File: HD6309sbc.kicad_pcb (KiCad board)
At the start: 2 copper layers, 99.8 x 99.8 mm, 30 parts, among them J1 Conn_01x02_Male, J2 Conn_02x30_Odd_Even, J3 Conn_01x02_Male, U1 HD63C09, U10 74LS375D, U11 74HC02, U12 74AHC1G08, U13 74HC21D, U14 74HC21D, U15 74HC21D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

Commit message: fixes
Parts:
- added R3: 4.7k, Resistor_SMD:R_0805_2012Metric_Pad1.20x1.40mm_HandSolder, F.Cu at (41.7, 109.0)
- added R4: 4.7k, Resistor_SMD:R_0805_2012Metric_Pad1.20x1.40mm_HandSolder, F.Cu at (41.7, 106.4)
- added R5: 4.7k, Resistor_SMD:R_0805_2012Metric_Pad1.20x1.40mm_HandSolder, F.Cu at (41.7, 103.9)
- added R6: 4.7k, Resistor_SMD:R_0805_2012Metric_Pad1.20x1.40mm_HandSolder, F.Cu at (41.7, 101.3)
- C1, C7: footprint Capacitor_SMD:C_0402_1005Metric -> Capacitor_SMD:C_0805_2012Metric_Pad1.18x1.45mm_HandSolder
- RN1, RN2, RN3: value R_Network08 -> 4K7
- U6: value 27C256 -> 28C256
- moved C7 0.68 mm to (123.7, 41.1)
- moved C1 0.66 mm to (108.0, 41.1)
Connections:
- U6 pad 1: unconnected-(U6-Pad1) -> +5V
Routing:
- net +5V: track 494.8 -> 518.7 mm
- net ~{NMI}: track 35.3 -> 56.3 mm, vias 0 -> 1
- net ~{IRQ}: track 40.8 -> 55.4 mm, vias 0 -> 1
- net ~{HALT}: track 39.7 -> 52.5 mm, vias 1 -> 2
- net ~{FIRQ}: track 44.7 -> 57.0 mm, vias 0 -> 1
- net A8: track 189.0 -> 193.5 mm

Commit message: rework traces
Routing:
- net A11: track 183.9 -> 178.0 mm, vias 1 -> 2
- net Net-(U13-Pad9): track 85.1 -> 86.5 mm
- net A1: track 157.9 -> 159.3 mm
- net D5: track 142.2 -> 143.1 mm
- net A8: track 193.5 -> 192.9 mm
- net D6: track 143.5 -> 144.0 mm
- net A0: track 186.8 -> 187.3 mm, vias 3 -> 5
- net GND: track 624.3 -> 624.9 mm
- net D0: track 148.0 -> 148.5 mm, vias 3 -> 5
- net A14: track 173.0 -> 172.6 mm, vias 4 -> 6
- net D1: track 151.2 -> 151.0 mm, vias 2 -> 3
- net A2: track 204.9 -> 204.7 mm, vias 3 -> 4
- net D2: track 168.3 -> 168.5 mm, vias 2 -> 4
- net +5V: track 518.7 -> 518.5 mm, vias 15 -> 17
- net A6: vias 6 -> 7
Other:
- board text added: "6309 SBC Rev 1.3"

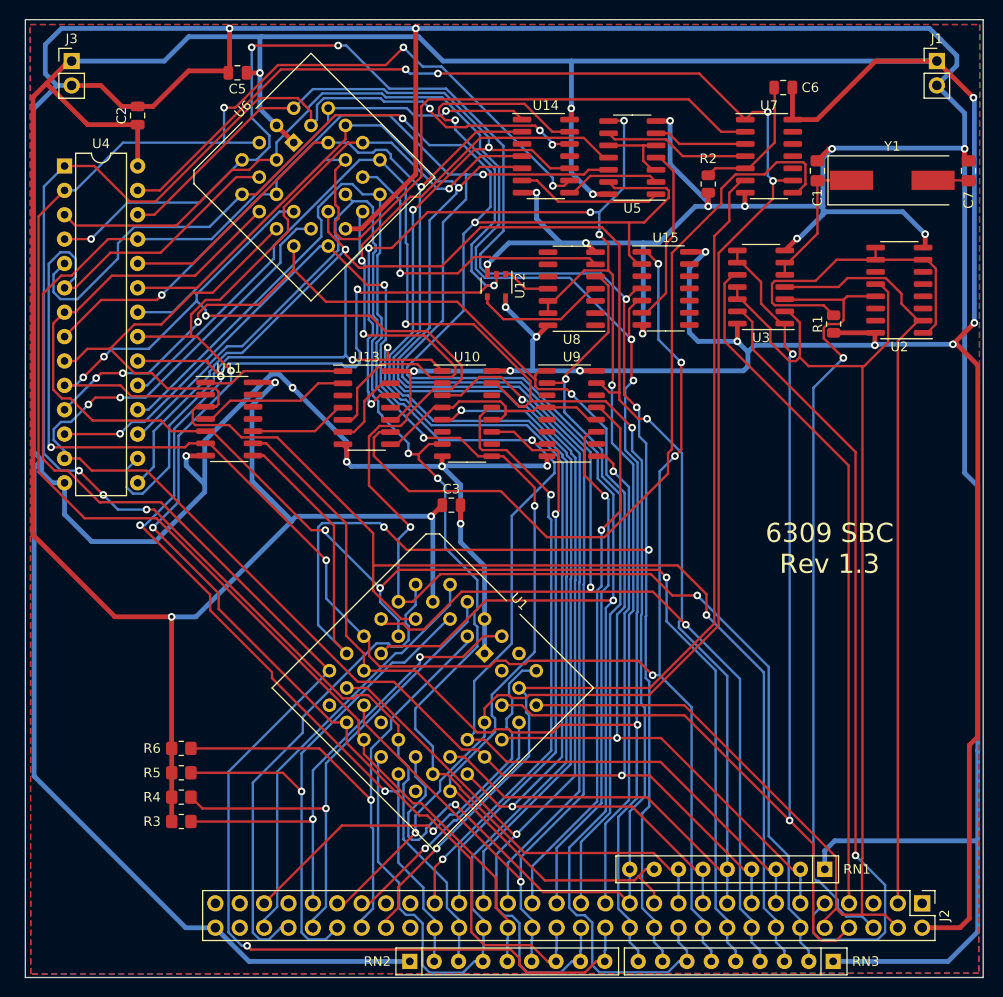
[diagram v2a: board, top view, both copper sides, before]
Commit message: use handsolder pads
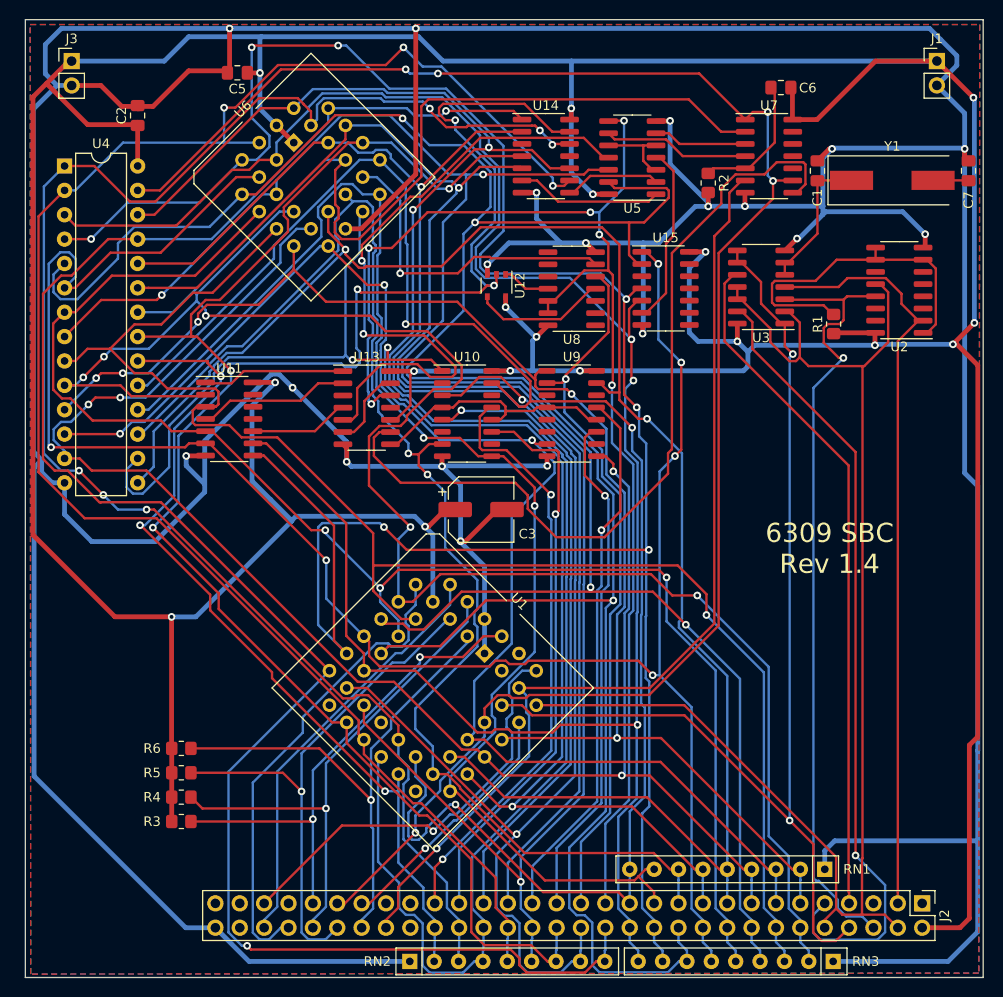
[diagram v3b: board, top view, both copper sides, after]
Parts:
- C1, C7: value 17pF -> 18pF
- C2, C5: footprint Capacitor_SMD:C_0805_2012Metric -> Capacitor_SMD:C_0805_2012Metric_Pad1.18x1.45mm_HandSolder
- C3: footprint Capacitor_SMD:C_0805_2012Metric -> Capacitor_SMD:CP_Elec_6.3x5.8
- C6: value C -> 1uF; footprint Capacitor_SMD:C_0805_2012Metric -> Capacitor_SMD:C_0805_2012Metric_Pad1.18x1.45mm_HandSolder
- R1, R2: footprint Resistor_SMD:R_0805_2012Metric -> Resistor_SMD:R_0805_2012Metric_Pad1.20x1.40mm_HandSolder
- moved C3 3.13 mm to (72.9, 76.5)
- moved C6 0.25 mm to (104.1, 32.5)
- moved R2 0.11 mm to (96.6, 42.4)
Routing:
- net GND: track 624.9 -> 629.0 mm
- net +5V: track 518.5 -> 519.6 mm
- net Net-(U13-Pad9): track 86.5 -> 87.4 mm
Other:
- board text added: "6309 SBC Rev 1.4"
- board text removed: "6309 SBC Rev 1.3"

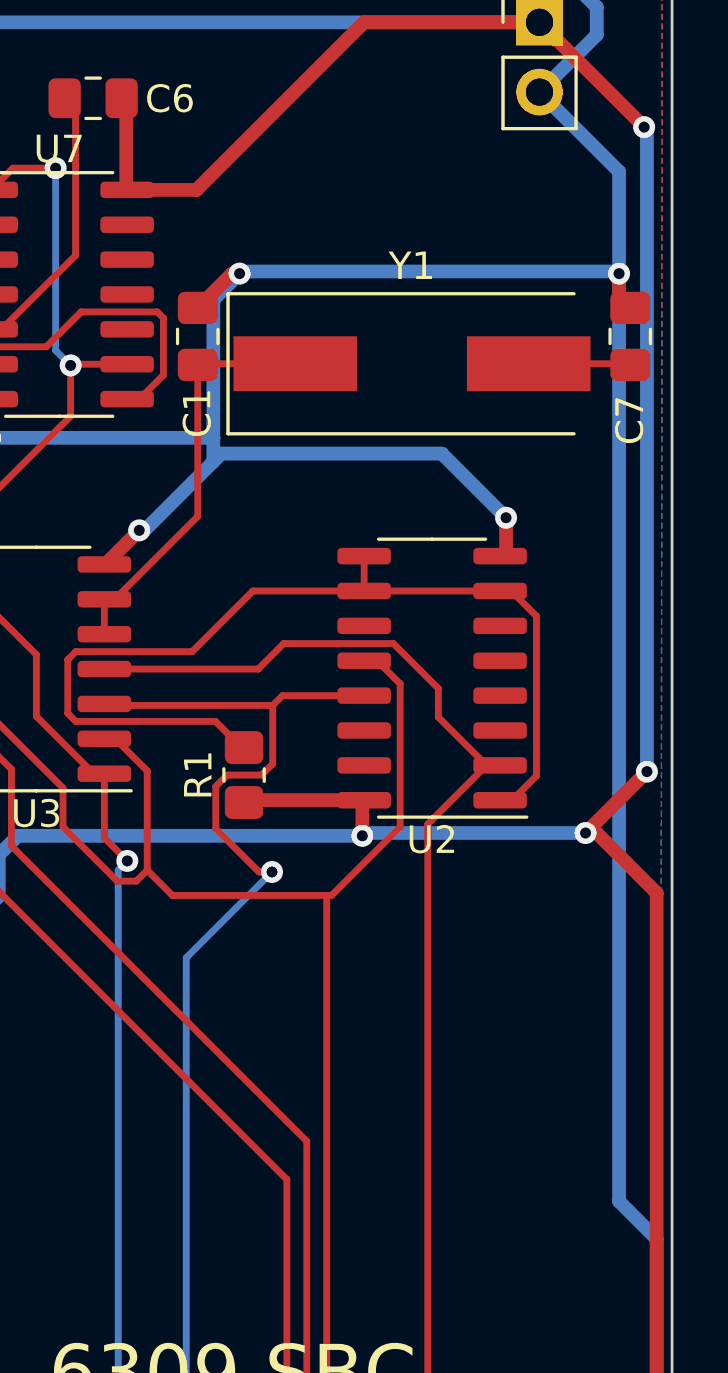
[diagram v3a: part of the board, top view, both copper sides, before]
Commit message: improve keepout around crystal
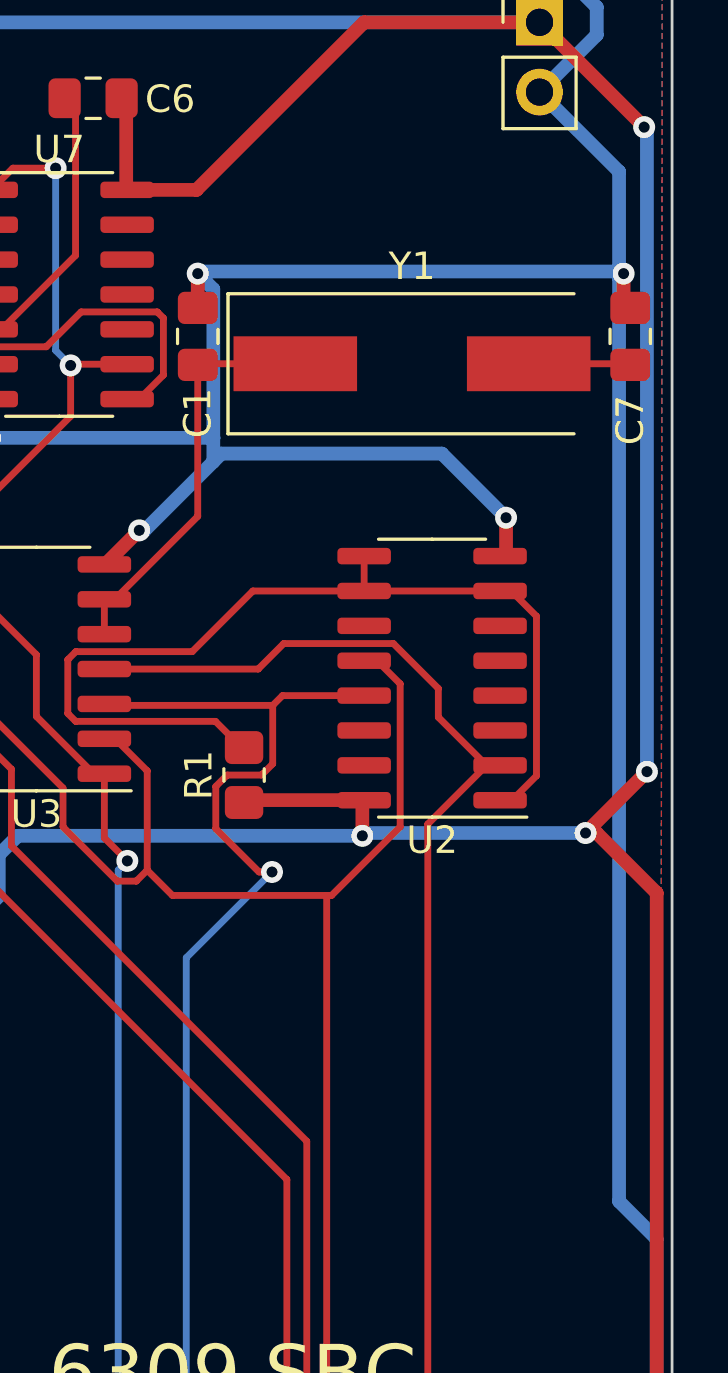
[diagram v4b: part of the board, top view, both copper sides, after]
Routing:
- net GND: track 629.0 -> 629.8 mm

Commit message: convert to discrete clock
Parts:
- removed C1, C7: 18pF, Capacitor_SMD:C_0805_2012Metric_Pad1.18x1.45mm_HandSolder
- removed R1: 2.2k, Resistor_SMD:R_0805_2012Metric_Pad1.20x1.40mm_HandSolder
- removed U2: 74HC163, Package_SO:SOIC-16_3.9x9.9mm_P1.27mm
- removed U3: 74HC02D, Package_SO:SOIC-14_3.9x8.7mm_P1.27mm
- removed Y1: 25.175MHz, Crystal:Crystal_SMD_HC49-SD
- added J4: Conn_01x06_Socket, Connector_PinSocket_2.54mm:PinSocket_1x06_P2.54mm_Vertical, F.Cu at (100.9, 78.4)
- added J5: Conn_01x06_Socket, Connector_PinSocket_2.54mm:PinSocket_1x06_P2.54mm_Vertical, F.Cu at (107.2, 50.3)
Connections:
- J2 pad 10: Clock3 -> Q
- U1 pad 39: Clock3 -> Q
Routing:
- net Q: track 0.00 -> 114.6 mm, vias 0 -> 2
- net Clock3: track 144.7 -> 61.3 mm, vias 0 -> 2
- net GND: track 629.8 -> 584.2 mm, vias 19 -> 15
- net Net-(R1-Pad2): track 36.2 -> 0.00 mm
- net Clock24: track 78.9 -> 53.1 mm, vias 0 -> 2
- net Clock6: track 82.8 -> 60.2 mm
- net ~{RESET}: track 102.5 -> 120.4 mm, vias 1 -> 3
- net Net-(C1-Pad1): track 15.0 -> 0.00 mm
- net ~{E}: track 71.7 -> 67.7 mm
- net +5V: track 519.6 -> 523.6 mm, vias 17 -> 13
- net Net-(C7-Pad1): track 3.71 -> 0.00 mm
- net E: track 114.8 -> 112.9 mm
- net ~{Q}: track 83.0 -> 84.8 mm
- net A4: track 208.1 -> 209.2 mm
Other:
- board text added: "1.5x"
- board text added: "12x"
- board text added: "24x"
- board text added: "3x"
- board text added: "6309 SBC Rev 1.5"
- board text added: "6x"
- board text added: "Clock Card"
- board text added: "E"
- board text added: "Q"
- board text added: "~{E}"
- board text added: "~{Q}"
- board text added: "~{RESET}"
- board text removed: "6309 SBC Rev 1.4"

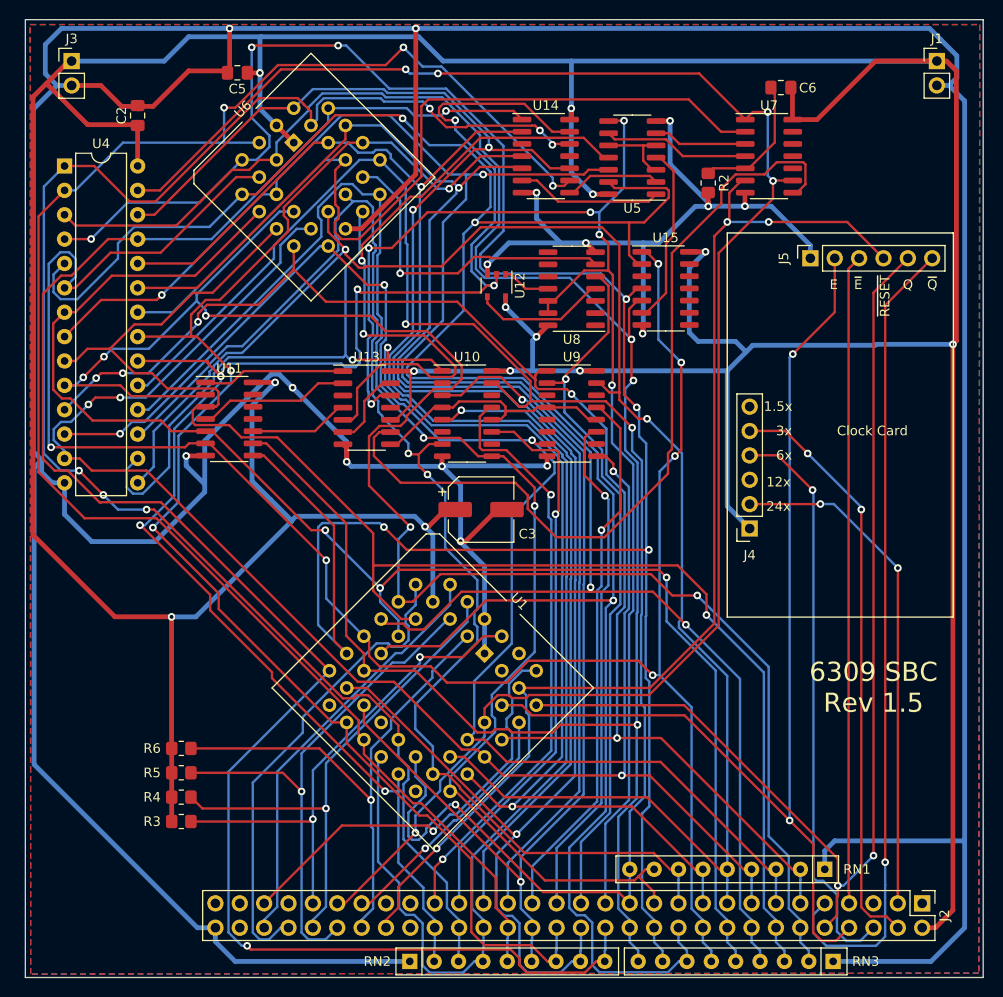
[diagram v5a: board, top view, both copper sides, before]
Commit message: add diagnostics port
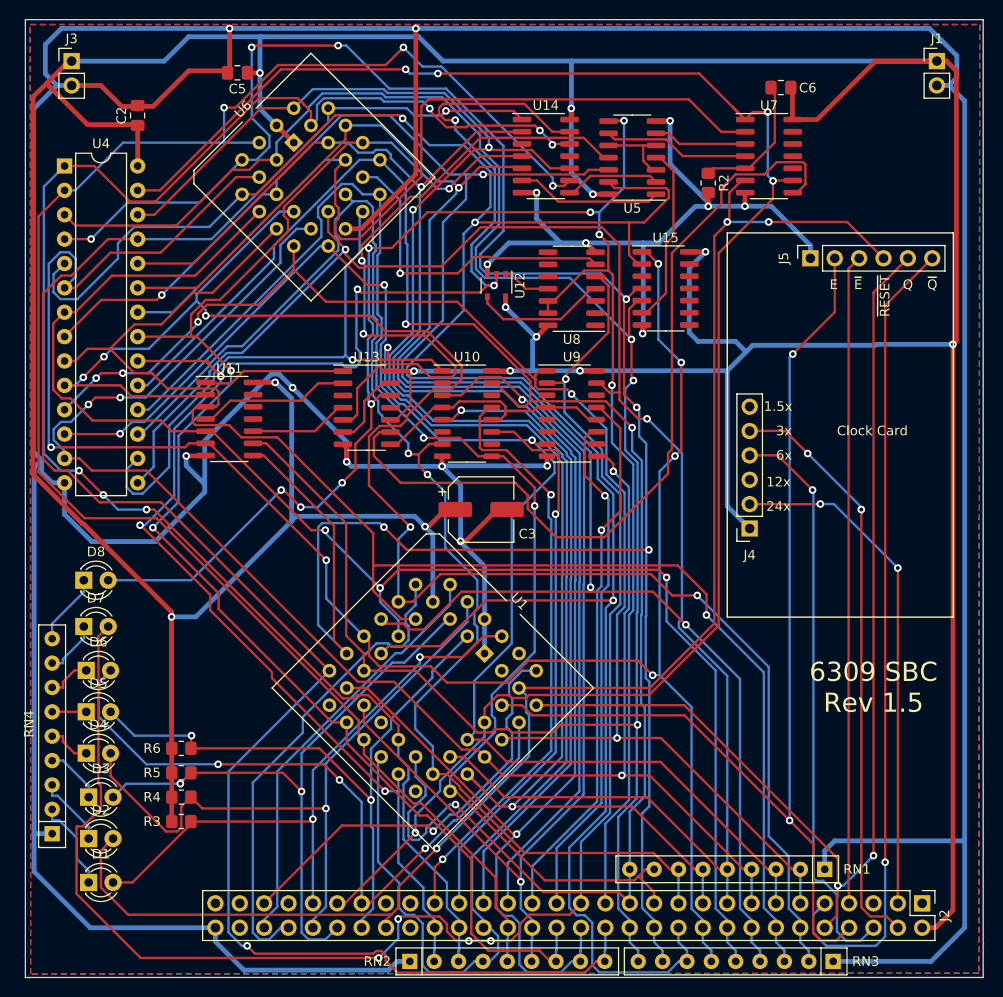
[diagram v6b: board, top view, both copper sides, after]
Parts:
- added D1: LED_Small, LED_THT:LED_D3.0mm, F.Cu at (32.0, 115.3)
- added D2: LED_Small, LED_THT:LED_D3.0mm, F.Cu at (32.0, 110.7)
- added D3: LED_Small, LED_THT:LED_D3.0mm, F.Cu at (32.0, 106.4)
- added D4: LED_Small, LED_THT:LED_D3.0mm, F.Cu at (31.7, 101.9)
- added D5: LED_Small, LED_THT:LED_D3.0mm, F.Cu at (31.7, 97.5)
- added D6: LED_Small, LED_THT:LED_D3.0mm, F.Cu at (31.7, 93.2)
- added D7: LED_Small, LED_THT:LED_D3.0mm, F.Cu at (31.5, 88.6)
- added D8: LED_Small, LED_THT:LED_D3.0mm, F.Cu at (31.5, 83.8)
- added RN4: 470R, Resistor_THT:R_Array_SIP9, F.Cu at (28.2, 110.2)
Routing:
- net ROM/~{RAM}: track 74.2 -> 166.2 mm, vias 1 -> 5
- net ~{DMA}: track 26.4 -> 73.4 mm, vias 1 -> 3
- net MAPPED_MEM: track 140.6 -> 180.1 mm, vias 6 -> 9
- net ~{RESET}: track 120.4 -> 157.4 mm
- net ~{IRQ}: track 55.2 -> 71.2 mm
- net ~{HALT}: track 52.5 -> 63.4 mm
- net ~{NMI}: track 56.1 -> 66.9 mm, vias 1 -> 2
- net ~{FIRQ}: track 56.8 -> 66.9 mm, vias 1 -> 2
- net Net-(D1-K): track 0.00 -> 9.61 mm
- net GND: track 584.2 -> 593.4 mm
- net Net-(D2-K): track 0.00 -> 7.50 mm
- net Net-(D8-K): track 0.00 -> 7.46 mm
- net Net-(D3-K): track 0.00 -> 6.10 mm
- net Net-(D7-K): track 0.00 -> 5.84 mm
- net +5V: track 523.6 -> 518.2 mm
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
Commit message: use 10 segment led bar
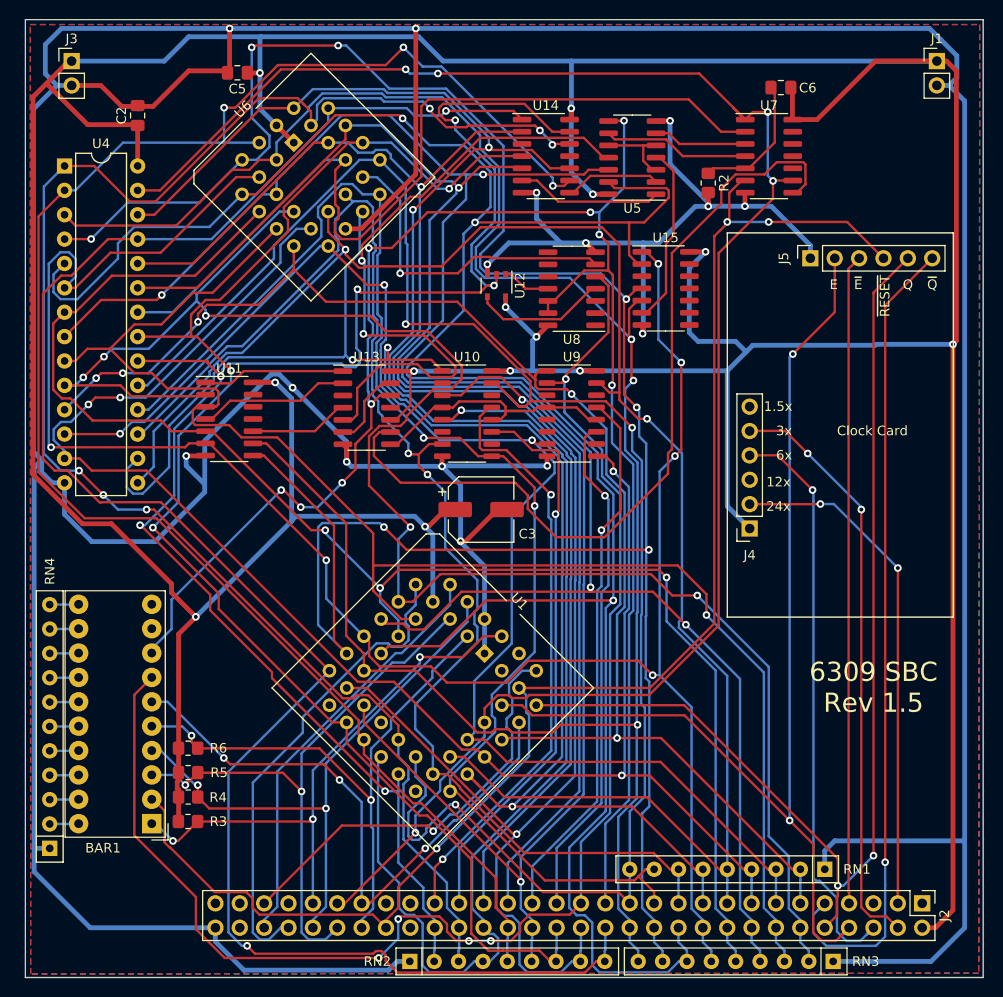
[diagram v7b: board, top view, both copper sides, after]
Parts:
- removed D1, D2, D3, D4, D5, D6, D7, D8: LED_Small, LED_THT:LED_D3.0mm
- added BAR1: HLCP-J100, Display:HLCP-J100, F.Cu at (38.6, 109.2)
- RN4: footprint Resistor_THT:R_Array_SIP9 -> Resistor_THT:R_Array_SIP11
- moved RN4 1.55 mm to (27.9, 111.8)
- moved R5 0.71 mm to (42.4, 103.9)
- moved R4 0.71 mm to (42.4, 106.4)
- moved R6 0.71 mm to (42.4, 101.3)
- moved R3 0.69 mm to (42.4, 109.0)
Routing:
- net ROM/~{RAM}: track 166.2 -> 151.8 mm
- net ~{DMA}: track 73.4 -> 63.1 mm
- net ~{IRQ}: track 71.2 -> 62.0 mm, vias 1 -> 2
- net Net-(BAR1A-K): track 9.61 -> 3.03 mm
- net ~{NMI}: track 66.9 -> 61.5 mm
- net ~{HALT}: track 63.4 -> 58.2 mm, vias 2 -> 3
- net ~{RESET}: track 157.4 -> 152.8 mm
- net Net-(BAR1B-K): track 7.50 -> 3.03 mm
- net Net-(BAR1H-K): track 7.46 -> 3.03 mm
- net ~{FIRQ}: track 66.9 -> 62.7 mm
- net Net-(BAR1C-K): track 6.10 -> 3.03 mm
- net Net-(BAR1J-K): track 0.00 -> 3.03 mm
- net Net-(BAR1I-K): track 0.00 -> 3.03 mm
- net Net-(BAR1G-K): track 5.84 -> 3.03 mm
- net Net-(BAR1D-K): track 4.63 -> 3.03 mm
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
